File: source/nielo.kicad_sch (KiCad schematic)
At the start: 0 parts

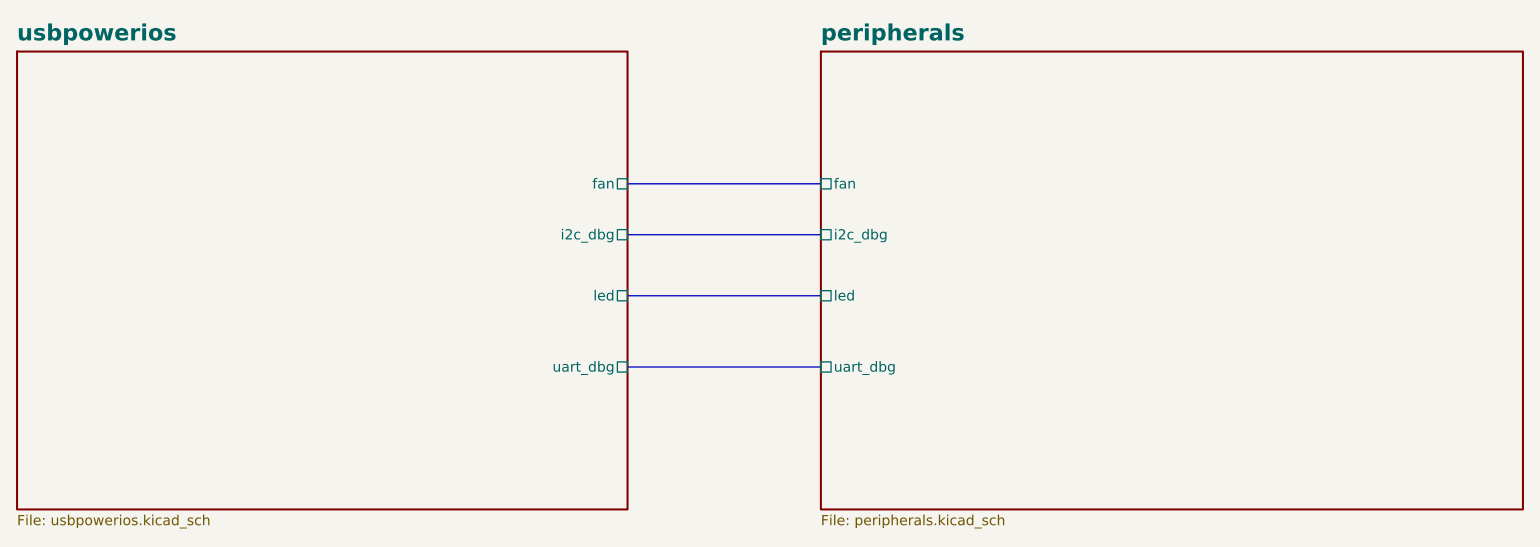
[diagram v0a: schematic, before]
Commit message: schematics r1 done, awaiting verification
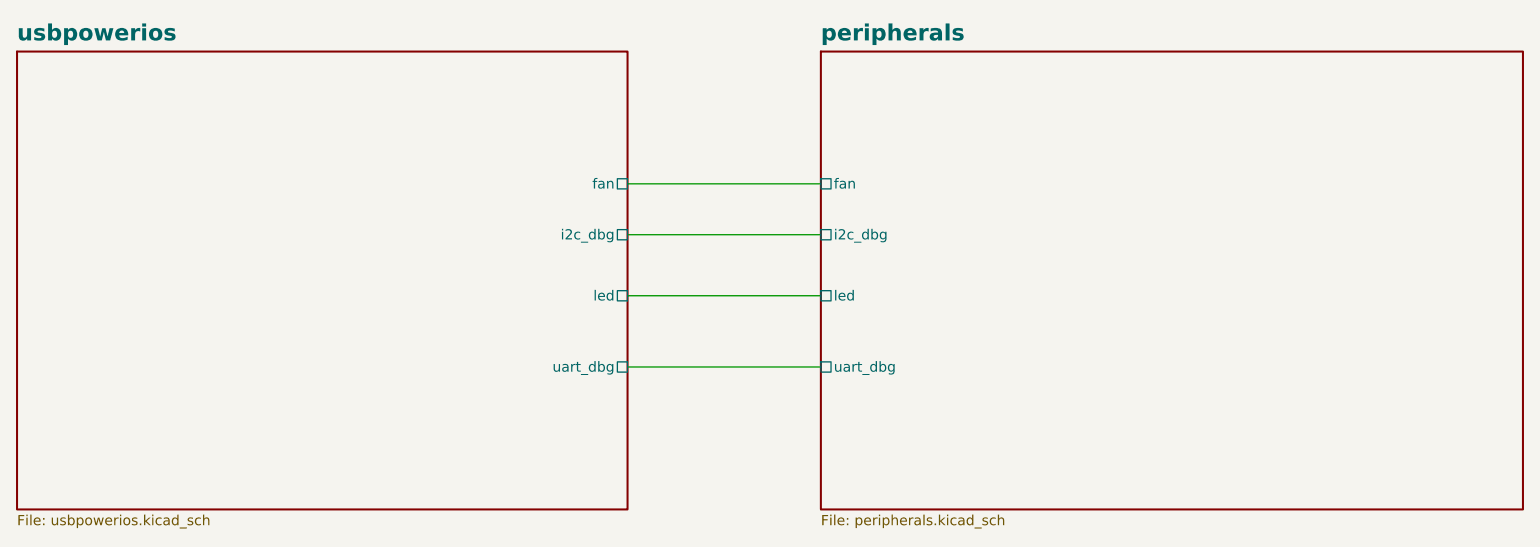
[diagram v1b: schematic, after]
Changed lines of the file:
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@@
 		(date "2026-09-20")
 	)
-	(bus
+	(wire
 		(pts
 			(xy 129.54 71.12) (xy 153.67 71.12)
@@
 		)
 	)
-	(bus
+	(wire
+		(pts
+			(xy 129.54 77.47) (xy 153.67 77.47)
+		)
+		(stroke
+			(width 0.508)
+			(type default)
+			(color 0 0 0 1)
+		)
+	)
+	(wire
 		(pts
 			(xy 129.54 93.98) (xy 153.67 93.98)
@@
 		)
 	)
-	(bus
-		(pts
-			(xy 129.54 77.47) (xy 153.67 77.47)
-		)
-		(stroke
-			(width 0.508)
-			(type default)
-			(color 0 0 0 1)
-		)
-	)
-	(bus
+	(wire
 		(pts
 			(xy 129.54 85.09) (xy 153.67 85.09)
@@
 				(font
 					(size 1.27 1.27)
+					(thickness 0.1588)
 				)
 				(justify left top)
@@
 				(font
 					(size 1.27 1.27)
+					(thickness 0.1588)
 				)
 				(justify left top)
